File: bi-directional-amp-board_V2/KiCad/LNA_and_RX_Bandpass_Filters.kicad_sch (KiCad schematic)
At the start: 31 parts

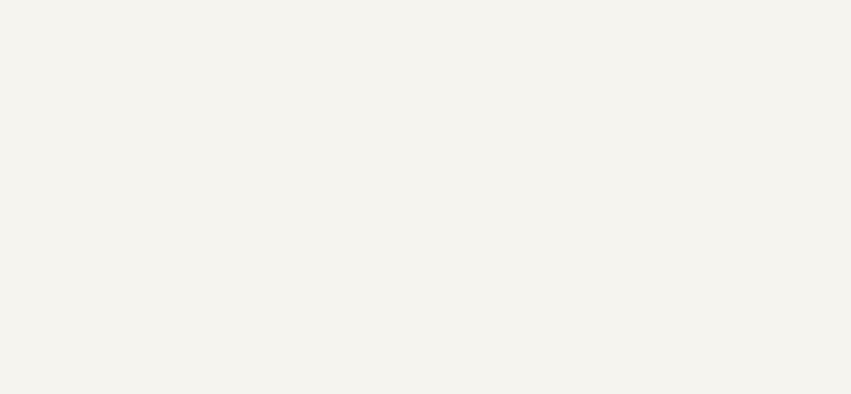
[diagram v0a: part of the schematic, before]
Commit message: re importing eagle files to kicad
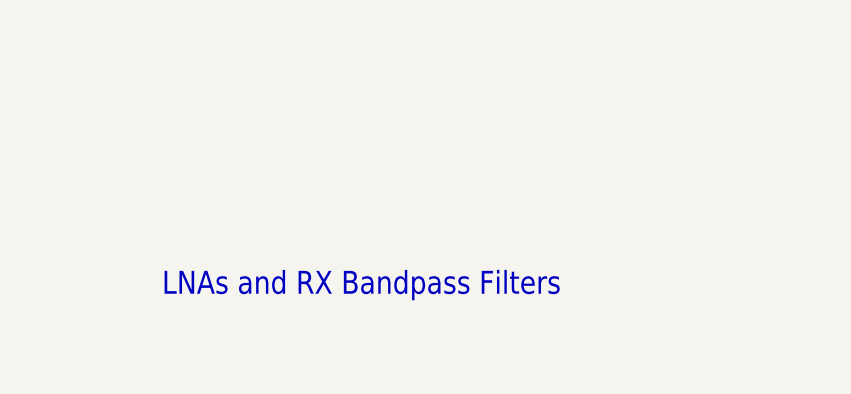
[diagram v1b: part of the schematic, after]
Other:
- note added: "LNAs and RX Bandpass Filters"
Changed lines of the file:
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@@
 (kicad_sch (version 20211123) (generator eeschema)
-  (paper "User" 490.22 254.406)
+  (paper "A2")
   (junction (at 127 80.01) (diameter 0) (color 0 0 0 0)
   )
@@
     (effects (font (size 1.778 1.5113)) (justify left bottom))
   )
+  (text "LNAs and RX Bandpass Filters" (at 210.82 205.74 180)
+    (effects (font (size 2.54 2.159)) (justify left bottom))
+  )
   (label "N$17" (at 177.8 160.02 0)

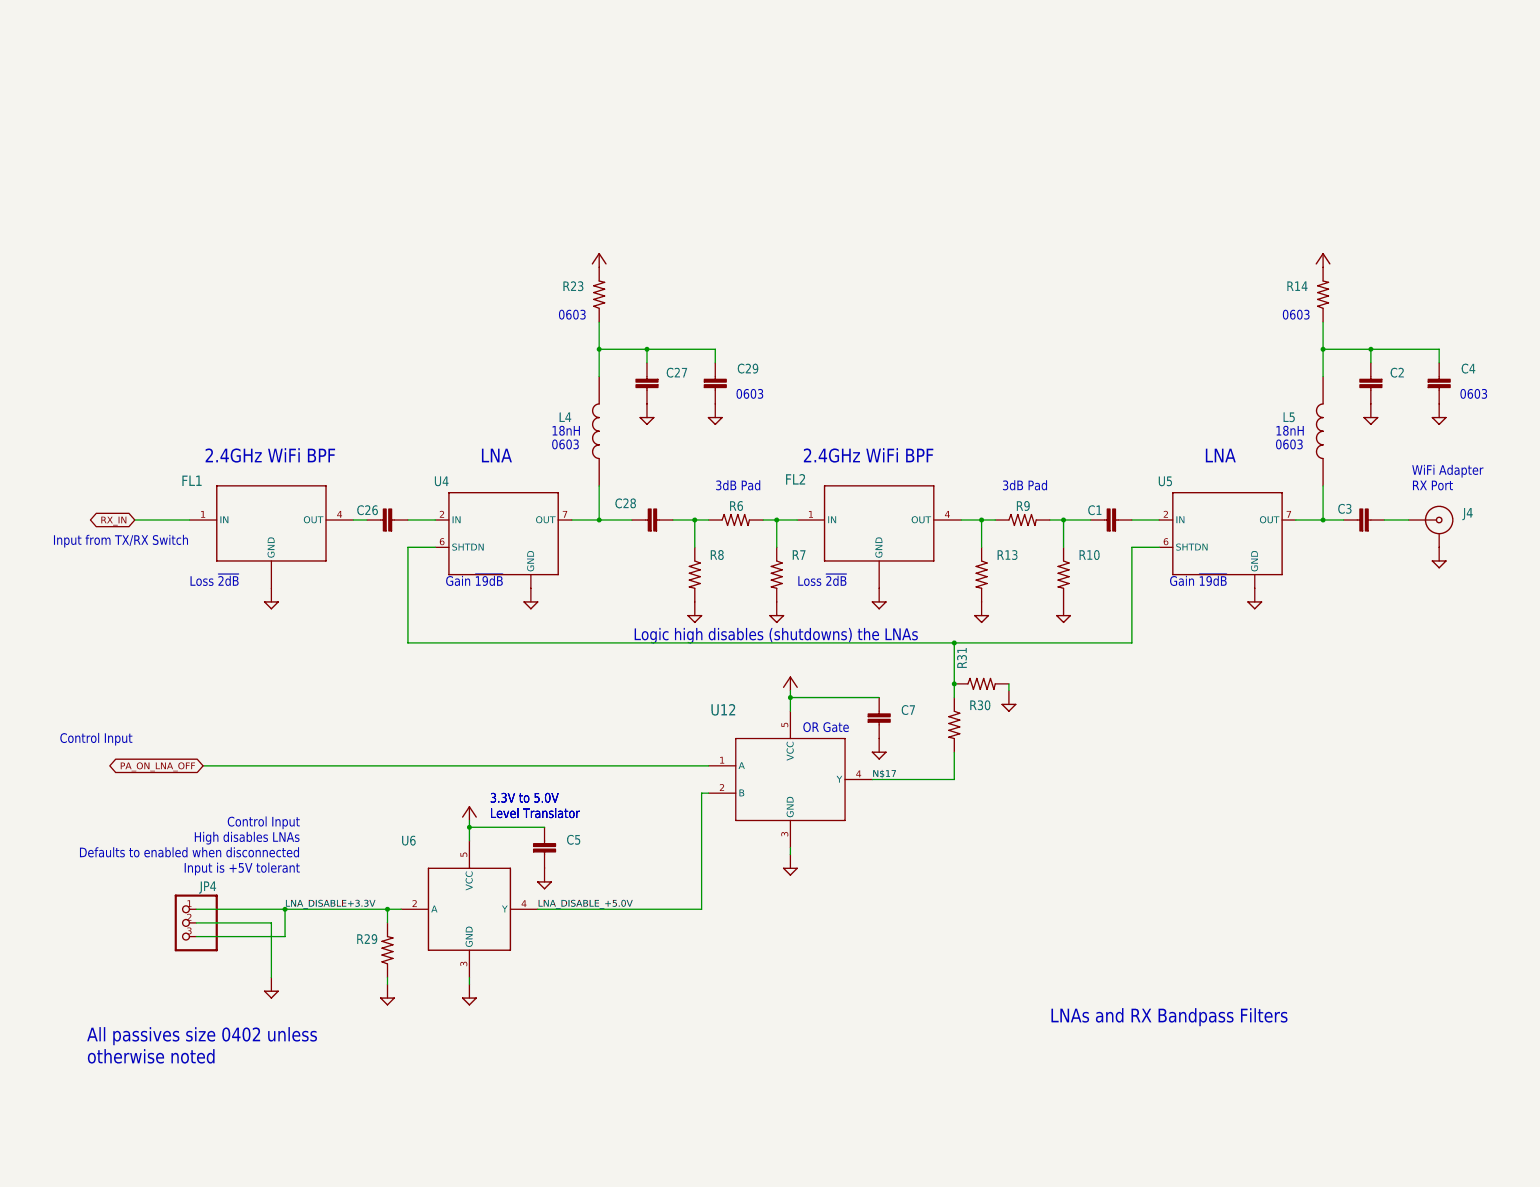
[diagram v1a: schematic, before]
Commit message: Updated KiCAD import of bidirectional amplifier. Still a bit broken, but better now.
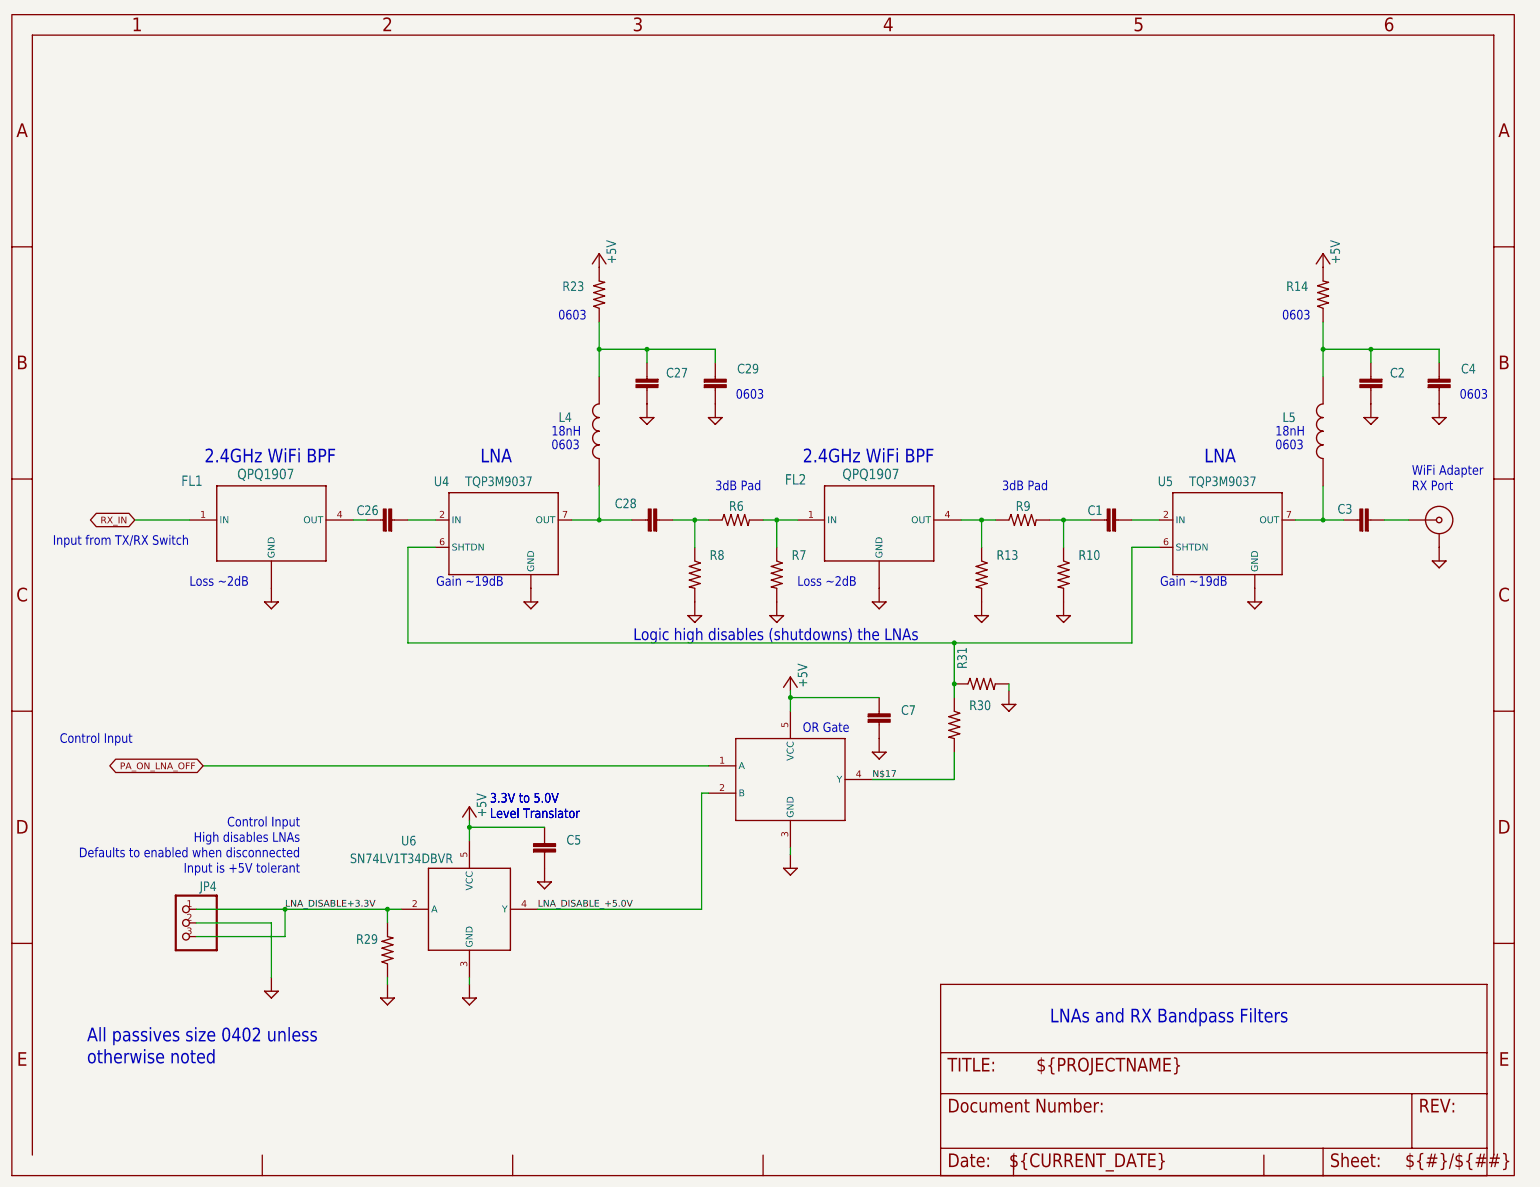
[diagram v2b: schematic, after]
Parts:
- C1, C26, C28, C3: value (none) -> C-EU0402-C-NOSILK; footprint (none) -> Bidirectional_Amp:.0402-C-NOSILK; MFR (none) -> Murata; MPN (none) -> GJM1555C1H150JB01D
- C2, C27: value (none) -> C-EU0402-B-NOSILK; footprint (none) -> Bidirectional_Amp:.0402-B-NOSILK; MFR (none) -> Murata; MPN (none) -> GJM1555C1H150JB01D
- C29, C4: value (none) -> C-EU0603-B-NOSILK; footprint (none) -> Bidirectional_Amp:.0603-B-NOSILK; MFR (none) -> KEMET; MPN (none) -> C0603X105M4RACAUTO
- C5: value (none) -> C-EU0402-B-NOSILK; footprint (none) -> Bidirectional_Amp:.0402-B-NOSILK; MFR (none) -> TDK Corporation; MPN (none) -> CGA2B1X7R1C104K050BC
- C7: value (none) -> C-EU0402-B-NOSILK; footprint (none) -> Bidirectional_Amp:.0402-B-NOSILK; MFR (none) -> TDK; MPN (none) -> CGA2B1X7R1C104K050BC
- FL1, FL2: value (none) -> QPQ1907; footprint (none) -> Bidirectional_Amp:FIL_B39162B9417K610; MPN (none) -> QPQ1907
- J4: value (none) -> 142-0701-851_ALT; footprint (none) -> Bidirectional_Amp:142-0701-851; MFR (none) -> Cinch; MPN (none) -> 142-0701-851
- JP4: value (none) -> PINHD-1X3; footprint (none) -> Bidirectional_Amp:1X03; MFR (none) -> Molex; MPN (none) -> 22-23-2031
- L4, L5: value (none) -> 68nH; footprint (none) -> Bidirectional_Amp:0603CS-68NXJLW; MPN (none) -> 0603CS-18NXJLW
- R10, R13, R7, R8: value (none) -> R-US_0402-C-NOSILK; footprint (none) -> Bidirectional_Amp:.0402-C-NOSILK; MFR (none) -> Panasonic; MPN (none) -> ERJ-2RKF2940X
- R14, R23: value (none) -> R-US_0603-B-NOSILK; footprint (none) -> Bidirectional_Amp:.0603-B-NOSILK; MFR (none) -> Panasonic; MPN (none) -> ERJ-3GEY0R00V
- R29: value (none) -> R-US_0402-B-NOSILK; footprint (none) -> Bidirectional_Amp:.0402-B-NOSILK; MFR (none) -> Panasonic; MPN (none) -> ERJ-2GEJ103X
- R30, R31: value (none) -> R-US_0402-B-NOSILK; footprint (none) -> Bidirectional_Amp:.0402-B-NOSILK; MFR (none) -> Panasonic; MPN (none) -> ERJ-2RKF2940X
- R6, R9: value (none) -> R-US_0402-C-NOSILK; footprint (none) -> Bidirectional_Amp:.0402-C-NOSILK; MFR (none) -> Panasonic; MPN (none) -> ERJ-2RKF17R8X
- U12: value (none) -> SN74LVC1G32DBVR; footprint (none) -> Bidirectional_Amp:DBV5
- U4, U5: value (none) -> TQP3M9037; footprint (none) -> Bidirectional_Amp:DFN8-2X2-WITH-PAD; MFR (none) -> Qorvo; MPN (none) -> TQP3M9037
- U6: value (none) -> SN74LV1T34DBVR; footprint (none) -> Bidirectional_Amp:SOT95P280X145-5N
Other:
- note added: "Gain ~19dB"
- note added: "Loss ~2dB"
- note removed: "Gain ~{19dB}"
- note removed: "Loss ~{2dB}"
